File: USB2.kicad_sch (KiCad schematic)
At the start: 18 parts, among them J1 USB_A

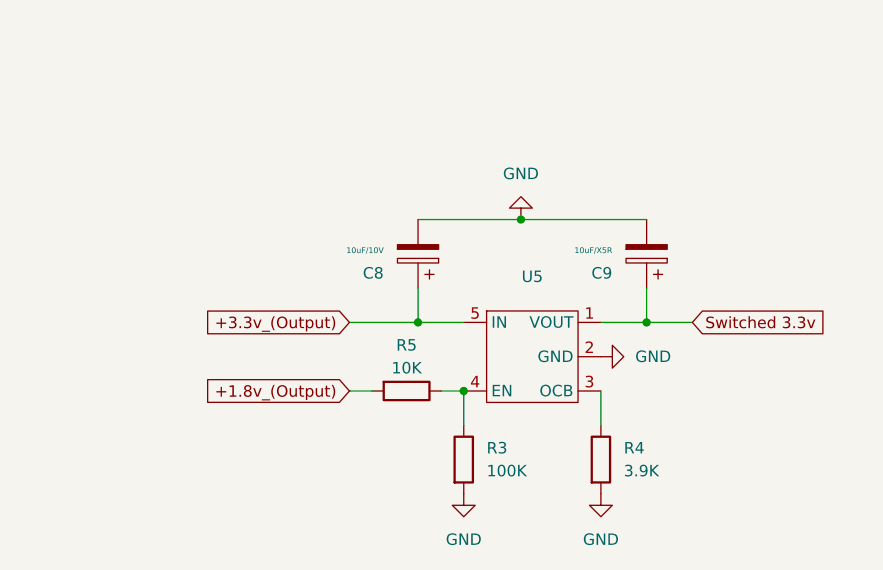
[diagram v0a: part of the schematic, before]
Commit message: usb3 down done
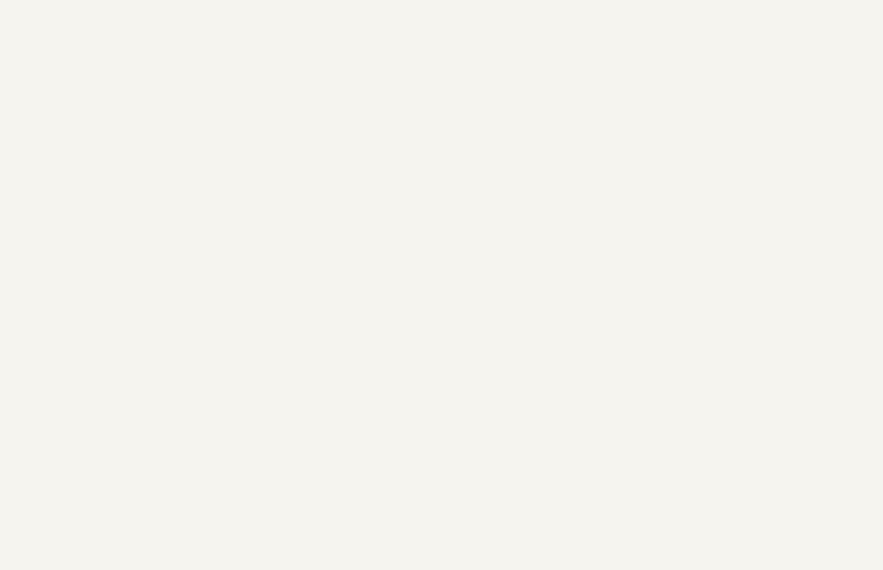
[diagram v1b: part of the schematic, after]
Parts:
- removed C8: 10uF/10V, symbol Device:C_Polarized
- removed C9: 10uF/X5R, symbol Device:C_Polarized
- removed R3: 100K, symbol Device:R
- removed R4: 3.9K, symbol Device:R
- removed R5: 10K, symbol Device:R
- removed U5: ~, symbol raxda:SGM2576YN5G/TR

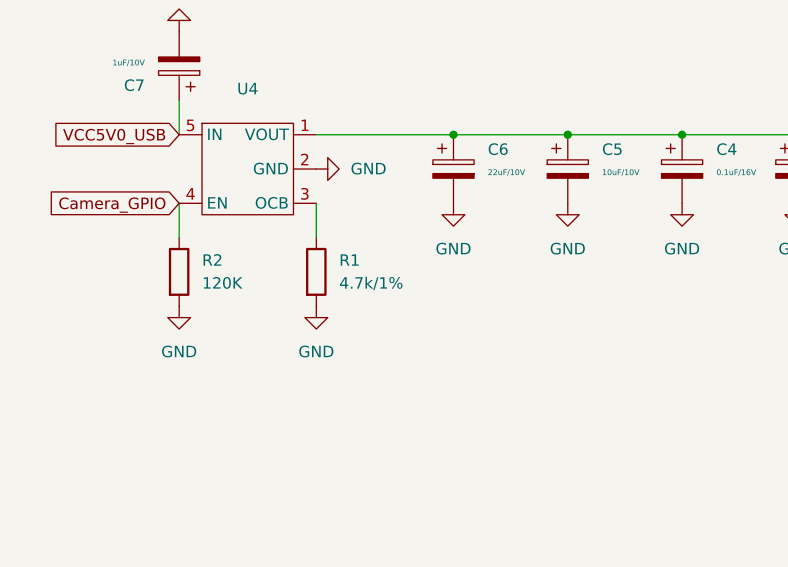
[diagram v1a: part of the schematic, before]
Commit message: finished usb3.0
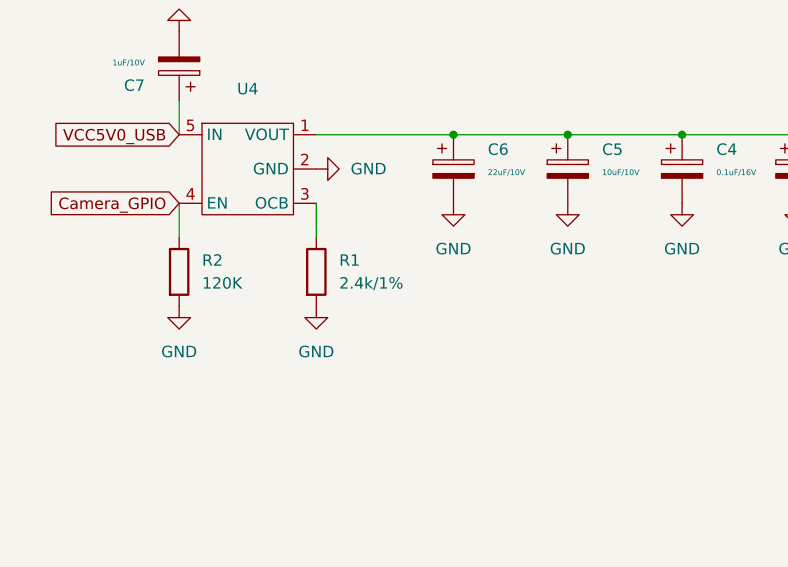
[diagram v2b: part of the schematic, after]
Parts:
- R1: value 4.7k/1% -> 2.4k/1%
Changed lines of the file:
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@@
 			)
 		)
-		(property "Value" "4.7k/1%"
+		(property "Value" "2.4k/1%"
 			(at 91.44 172.7199 0)
 			(effects

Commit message: Ethernet and MIPI cam done, USBC OTG started
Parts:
- D1, D2: footprint Diode_SMD:Infineon_SG-WLL-2-3_0.58x0.28_P0.36mm -> radxa:DFN1006-2L
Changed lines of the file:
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@@
 			)
 		)
-		(property "Footprint" "Diode_SMD:Infineon_SG-WLL-2-3_0.58x0.28_P0.36mm"
+		(property "Footprint" "radxa:DFN1006-2L"
 			(at 171.45 186.69 0)
 			(effects
@@
 			)
 		)
-		(property "Footprint" "Diode_SMD:Infineon_SG-WLL-2-3_0.58x0.28_P0.36mm"
+		(property "Footprint" "radxa:DFN1006-2L"
 			(at 173.99 193.04 0)
 			(effects

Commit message: usbc work
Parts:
- FL1: value MCZ1210AH900L2TD0G -> MCZ1210DH120L2TA0G
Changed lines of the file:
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@@
 			)
 		)
-		(property "Value" "MCZ1210AH900L2TD0G"
+		(property "Value" "MCZ1210DH120L2TA0G"
 			(at 188.087 175.26 0)
 			(effects

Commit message: usbc work
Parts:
- U4: value ~ -> SGM2576
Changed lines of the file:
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@@
 		(fields_autoplaced yes)
 		(property "Reference" "U4"
-			(at 81.28 151.13 0)
+			(at 81.28 149.86 0)
 			(effects
 				(font
@@
 			)
 		)
-		(property "Value" "~"
-			(at 81.28 153.67 0)
+		(property "Value" "SGM2576"
+			(at 81.28 152.4 0)
 			(effects
 				(font
